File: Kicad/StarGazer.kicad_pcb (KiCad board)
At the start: 4 copper layers, 99.9 x 99.9 mm, 107 parts, among them J201 USB_B_Micro, J202 JST - 2x1, J203 Conn_01x01, J204 Conn_01x01, J301 JST - 4x1, J302 JST - 4x1, J303 JST - 5x1, J304 JST - 5x1, SW201 JST - 2x1, SW301 RESET PUSH, U101 STM32G070KBT6, U201 STBC08, U202 AP22811BW5-7, U203 TLV75528PDBVR, U301 TSX-3225, U302 LIS3MDLTR, U303 LSM6DS33TR, U304 74HC595PW,112, U305 74HC595PW,112, U306 74HC595PW,112

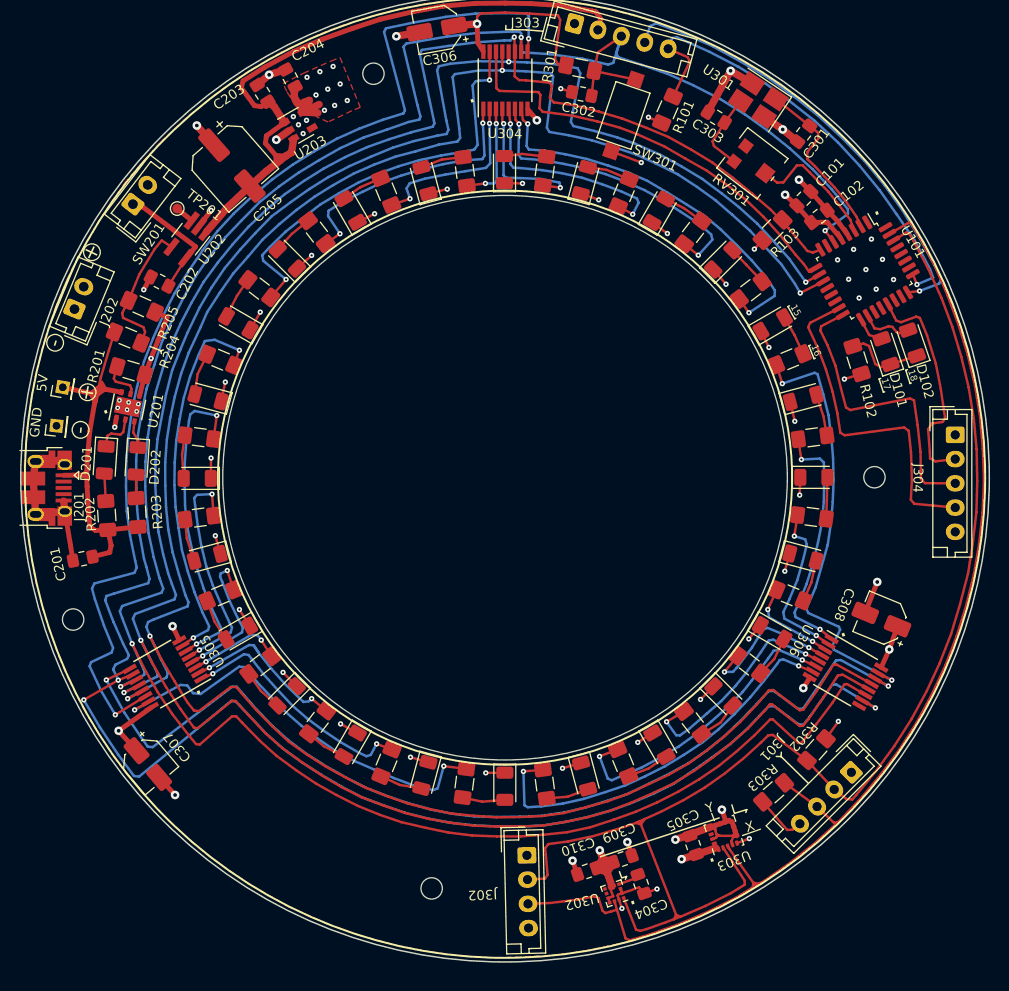
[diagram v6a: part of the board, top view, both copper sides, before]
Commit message: PCB is likely complete.  Added USART for GPS.  Added background art and front label. Some leftover things are needed for the case.
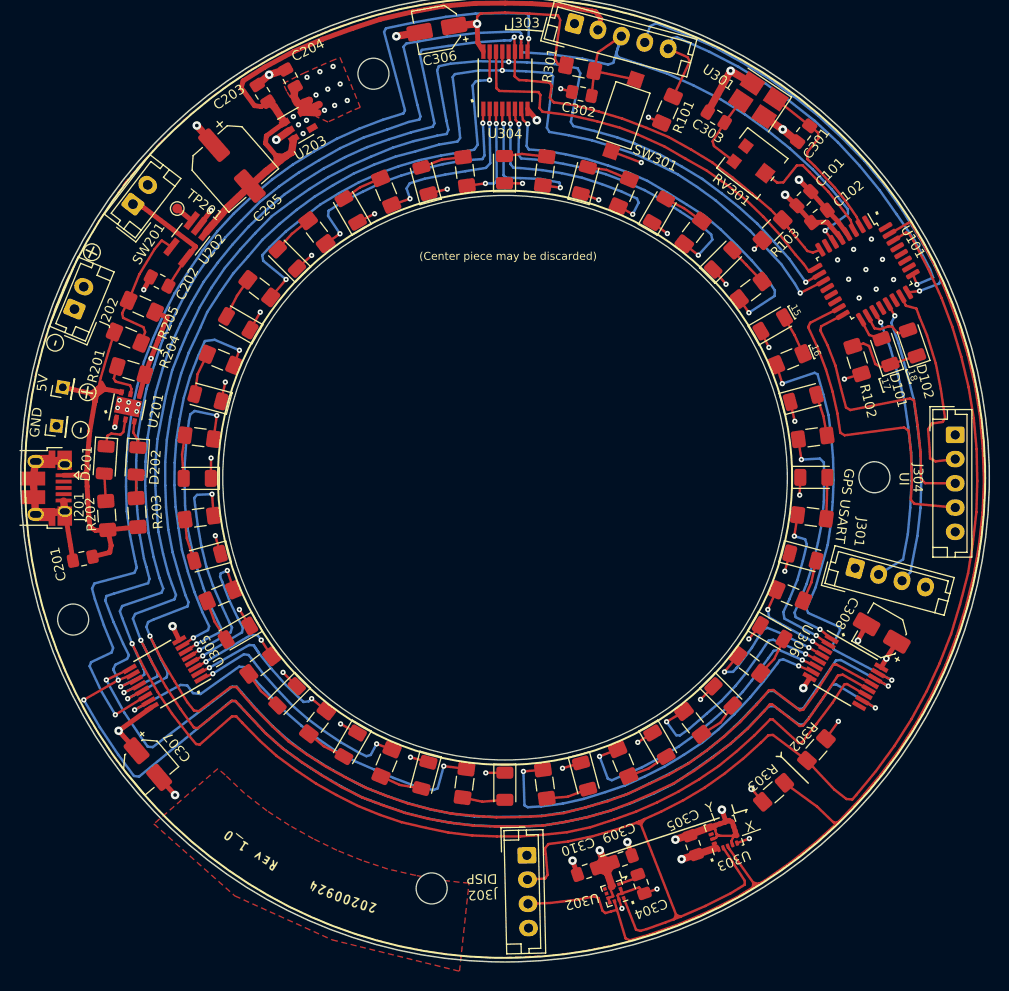
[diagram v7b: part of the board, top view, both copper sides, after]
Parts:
- removed the G*** at (160.0, 89.9)
- added G***: LOGO, Kicad:Back_Art, B.Cu at (159.6, 89.5)
- added G***: LOGO, Kicad:Label_Date_Rev, F.Cu at (138.8, 130.9)
- added G***: LOGO, Kicad:Label_URL, F.Cu at (137.4, 131.6)
- added G***: LOGO, Kicad:Label_Name, F.Cu at (139.8, 128.6)
- H101, H102, H103, H104: footprint MountingHole:MountingHole_2.2mm_M2 -> MountingHole:MountingHole_3.2mm_M3
- moved J301 21.0 mm to (196.1, 99.3), turned to 345 degrees
- moved C308 1.38 mm to (198.8, 105.9), turned to 150.1 degrees
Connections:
- J301 pad 2: I2C_SCL -> USART1_TX
- J301 pad 3: I2C_SDA -> USART1_RX
- R103 pad 1: (no net) -> SHIFT_REG_CLK
- U101 pad 19: (no net) -> USART1_TX
- U101 pad 21: UI_BUTTON -> USART1_RX
- U101 pad 23: (no net) -> UI_BUTTON
- U201 pad 7: (no net) -> GND
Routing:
- net USART1_RX: track 0.00 -> 29.6 mm, vias 0 -> 1
- net USART1_TX: track 0.00 -> 29.1 mm, vias 0 -> 1
- net V_REG: track 74.4 -> 69.3 mm, vias 17 -> 18
- net GND: track 154.4 -> 152.9 mm, vias 50 -> 56
- net UI_BUTTON: track 23.2 -> 21.9 mm
- net SHIFT_REG_CLK: track 233.3 -> 234.4 mm
- net (no net): vias 19 -> 13
- added copper zone on F.Cu, net (none)
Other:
- board text added: "(Center piece may be discarded)"
- board text added: "DISP"
- board text added: "GPS USART"
- board text added: "UI"

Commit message: Purchases made, case ordered, PCB ordered, parts ordered, money not happy.
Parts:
- removed C309: 100nF, Capacitor_SMD:C_0805_2012Metric_Pad1.15x1.40mm_HandSolder
- removed C310: 1uF, Capacitor_SMD:C_0805_2012Metric_Pad1.15x1.40mm_HandSolder
- C304: value 100nF -> 2.2uF
- U302: value LIS3MDLTR -> MMC5603NJ; footprint Package_LGA:LGA-12_2x2mm_P0.5mm -> Kicad:BGA_2_2
- moved U302 3.71 mm to (173.0, 129.5), turned to 109 degrees
- moved H102 3.53 mm to (155.9, 132.4)
- moved G*** 0.88 mm to (139.5, 131.3), turned to 152 degrees
- moved G*** 0.73 mm to (138.1, 131.5), turned to 152 degrees
- moved G*** 0.57 mm to (160.0, 89.9)
- moved G*** 0.44 mm to (140.2, 128.4), turned to 152 degrees
- moved C304 0.39 mm to (173.9, 132.2), turned to 22.5 degrees
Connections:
- C304 pad 2: Net-(C304-Pad2) -> V_REG
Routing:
- net I2C_SDA: track 122.8 -> 132.2 mm
- net V_REG: track 69.3 -> 60.9 mm
- net I2C_SCL: track 140.4 -> 134.7 mm
- net GND: track 152.9 -> 147.8 mm, vias 56 -> 53
- net Net-(C304-Pad2): track 2.29 -> 0.00 mm
